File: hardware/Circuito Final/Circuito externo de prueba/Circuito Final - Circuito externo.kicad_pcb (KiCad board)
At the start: 2 copper layers, 163.8 x 129.8 mm, 18 parts, among them J1 Conn_02x19_Odd_Even, J2 Conn_02x19_Odd_Even, J3 Conn_01x02, J4 Conn_01x02, J5 Conn_01x02_Socket, SW1 SW_DIP_x04, SW2 SW_DIP_x04, SW4 SW_DIP_x01, SW5 SW_DIP_x01, SW6 SW_DIP_x01

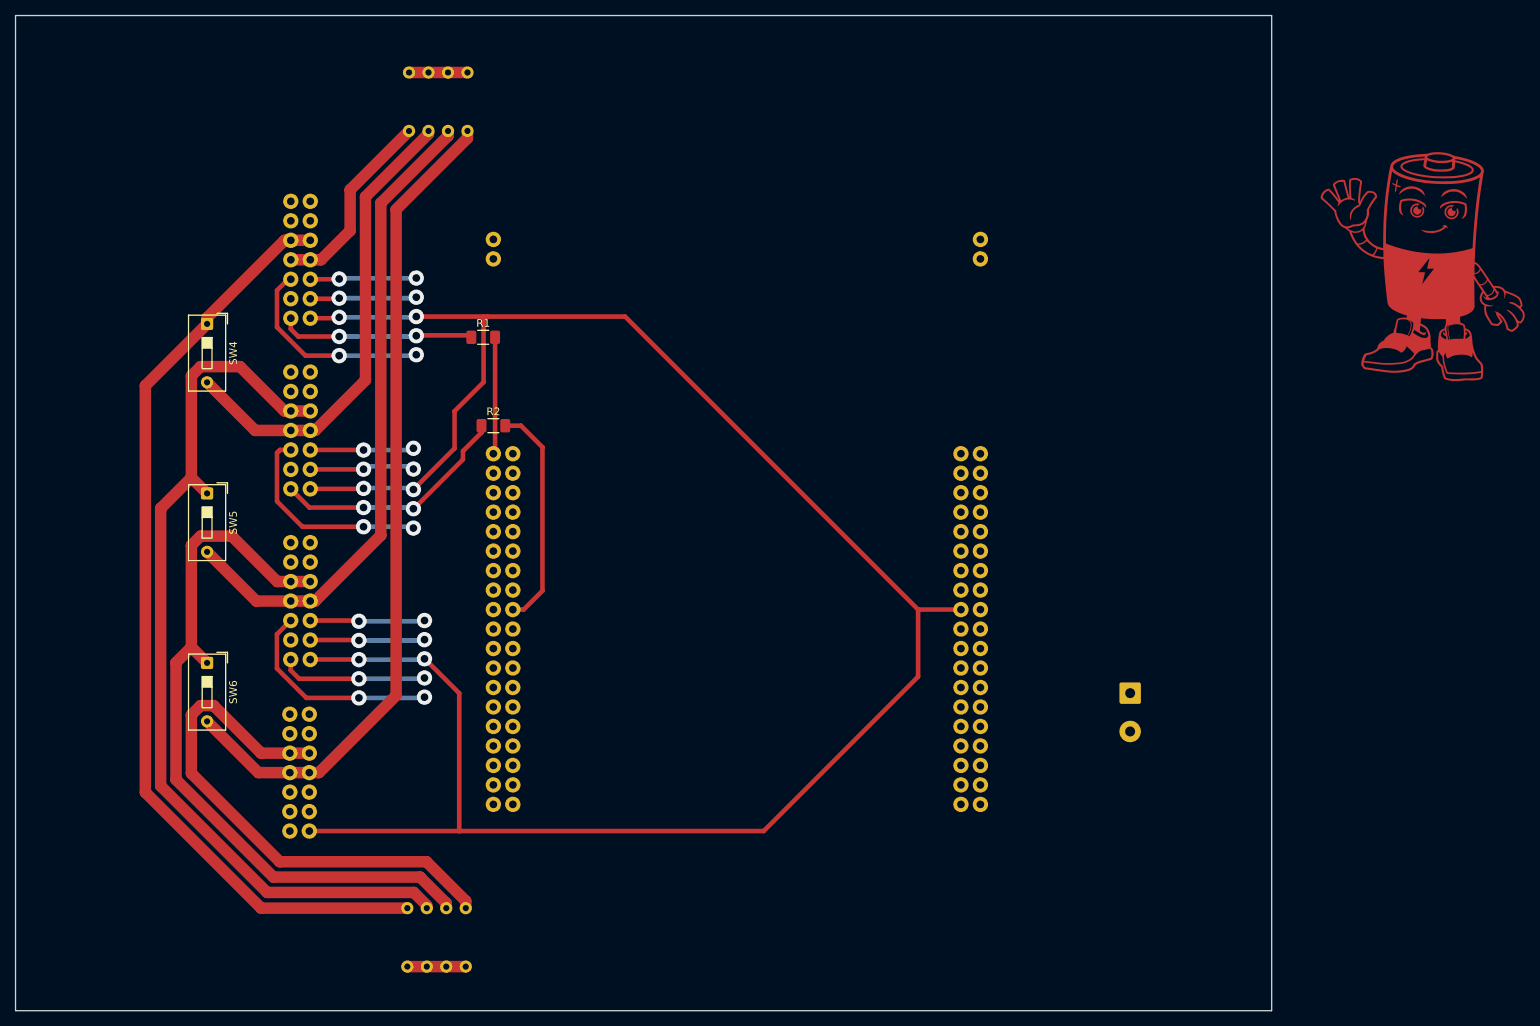
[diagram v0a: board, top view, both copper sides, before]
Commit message: subida de mediciones de switcheo con dos bancos, bitacora y kicad del circuito externo de prueba terminado
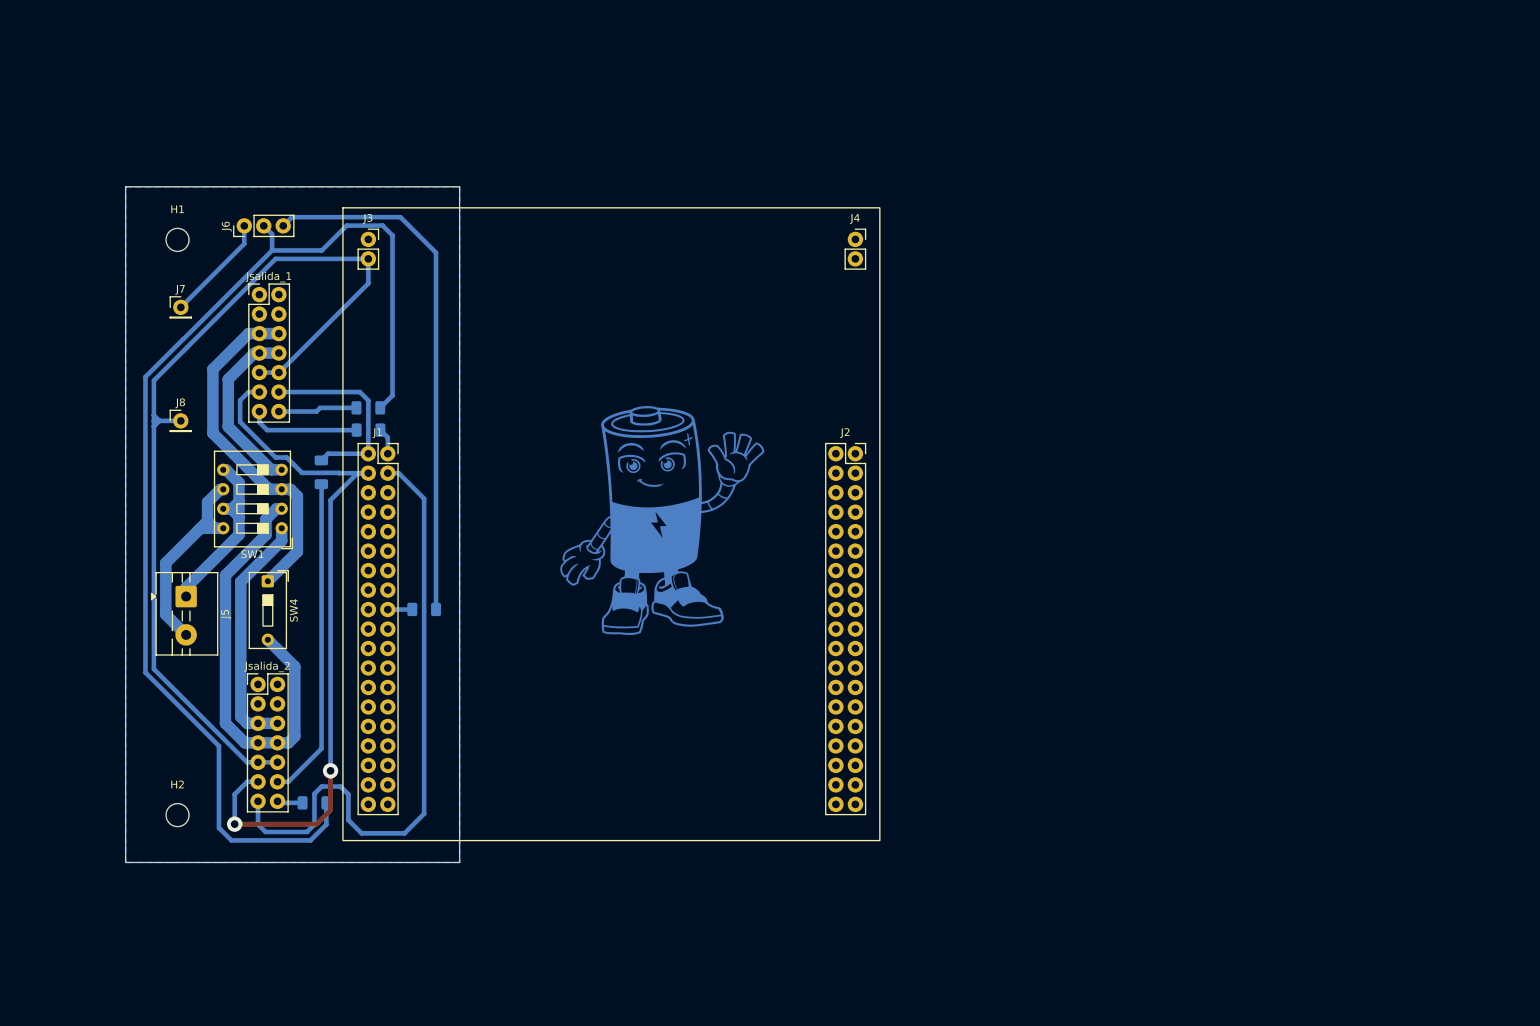
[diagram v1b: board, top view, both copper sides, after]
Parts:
- removed Jsalida_3, Jsalida_4: Conn_02x07_Odd_Even, Connector_PinHeader_2.54mm:PinHeader_2x07_P2.54mm_Vertical
- removed SW2: SW_DIP_x04, Button_Switch_THT:SW_DIP_SPSTx04_Slide_6.7x11.72mm_W7.62mm_P2.54mm_LowProfile
- removed SW5, SW6: SW_DIP_x01, Button_Switch_THT:SW_DIP_SPSTx01_Slide_9.78x4.72mm_W7.62mm_P2.54mm
- added H1: MountingHole, MountingHole:MountingHole_3mm, F.Cu at (73.1, 47.1)
- added H2: MountingHole, MountingHole:MountingHole_3mm, F.Cu at (73.1, 122.1)
- added J6: Conn_01x03_Pin, Connector_PinHeader_2.54mm:PinHeader_1x03_P2.54mm_Vertical, F.Cu at (81.8, 45.3)
- added J7: Conn_01x01, Connector_PinHeader_2.54mm:PinHeader_1x01_P2.54mm_Vertical, F.Cu at (73.5, 55.9)
- added J8: Conn_01x01, Connector_PinHeader_2.54mm:PinHeader_1x01_P2.54mm_Vertical, F.Cu at (73.5, 70.7)
- added R3: 0, Resistor_SMD:R_1206_3216Metric_Pad1.30x1.75mm_HandSolder, B.Cu at (98.0, 69.0)
- added R4: 0, Resistor_SMD:R_1206_3216Metric_Pad1.30x1.75mm_HandSolder, B.Cu at (105.3, 95.3)
- added R5: 0, Resistor_SMD:R_1206_3216Metric_Pad1.30x1.75mm_HandSolder, B.Cu at (91.0, 120.5)
- G***, R1, R2: moved to B.Cu
- J1, J2, J3, J4, J5, Jsalida_1, Jsalida_2, STM32: moved to F.Cu
- SW1: footprint Button_Switch_THT:SW_DIP_SPSTx04_Slide_6.7x11.72mm_W7.62mm_P2.54mm_LowProfile -> Button_Switch_THT:SW_DIP_SPSTx04_Slide_9.78x12.34mm_W7.62mm_P2.54mm; moved to F.Cu
- moved J5 123.7 mm to (74.2, 93.6)
- moved G*** 105.0 mm to (136.1, 84.0), turned to 180 degrees
- moved J3 79.8 mm to (98.0, 47.0), turned to 0 degrees
- moved J1 74.7 mm to (100.5, 75.0), turned to 0 degrees
- moved SW1 52.2 mm to (86.7, 84.7), turned to 180 degrees
- moved J2 47.2 mm to (161.5, 75.0), turned to 0 degrees
- moved J4 47.2 mm to (161.5, 47.0), turned to 0 degrees
- moved Jsalida_2 41.3 mm to (83.6, 105.1), turned to 0 degrees
- moved SW4 34.5 mm to (84.9, 91.6)
- moved R1 27.5 mm to (91.9, 77.4), turned to 90 degrees
- moved STM32 16.4 mm to (129.7, 84.2), turned to 0 degrees
- moved R2 16.3 mm to (98.0, 71.9), turned to 180 degrees
- moved Jsalida_1 13.9 mm to (83.8, 54.2), turned to 0 degrees
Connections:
- J1 pad 1: unconnected-(J1-Pin_1-Pad1) -> /Data_1
- J1 pad 17: /Vcc -> /Vcc_placa
- J1 pad 19: GND -> unconnected-(J1-Pin_19-Pad19)
- J1 pad 2: /Data_3 -> /clk_shift
- J1 pad 20: GND -> unconnected-(J1-Pin_20-Pad20)
- J1 pad 21: GND -> unconnected-(J1-Pin_21-Pad21)
- J1 pad 3: unconnected-(J1-Pin_3-Pad3) -> /Data_2
- J1 pad 4: /Data_4 -> /clk_latch
- J1 pad 7: GND -> unconnected-(J1-Pin_7-Pad7)
- J2 pad 1: /Data_1 -> unconnected-(J2-Pin_1-Pad1)
- J2 pad 10: GND -> unconnected-(J2-Pin_10-Pad10)
- J2 pad 18: /Data_2 -> unconnected-(J2-Pin_18-Pad18)
- J2 pad 19: GND -> unconnected-(J2-Pin_19-Pad19)
- J2 pad 3: /clk_shift -> unconnected-(J2-Pin_3-Pad3)
- J2 pad 31: GND -> unconnected-(J2-Pin_31-Pad31)
- J2 pad 5: /clk_latch -> unconnected-(J2-Pin_5-Pad5)
- J4 pad 2: GND -> unconnected-(J4-Pin_2-Pad2)
- Jsalida_1 pad 12: unconnected-(Jsalida_1-Pin_12-Pad12) -> /clk_shift
- Jsalida_1 pad 13: /Vcc -> /Data_1
- Jsalida_1 pad 14: /Data_1 -> /Vcc
- Jsalida_1 pad 9: /clk_shift -> GND
- Jsalida_2 pad 12: unconnected-(Jsalida_2-Pin_12-Pad12) -> /clk_shift
- Jsalida_2 pad 13: /Vcc -> /Data_2
- Jsalida_2 pad 14: /Data_2 -> /Vcc
- Jsalida_2 pad 9: /clk_shift -> GND
- R1 pad 1: /Data_1 -> /clk_shift
- R1 pad 2: /Data_1 -> /clk_shift
- R2 pad 1: /Data_2 -> /Data_1
- R2 pad 2: /Data_2 -> /Data_1
- SW1 pad 1: /bus_pos_1 -> /bus_pos_2
- SW1 pad 2: /bus_pos_2 -> /bus_neg_2
- SW1 pad 3: /bus_pos_3 -> /bus_pos_1
- SW1 pad 4: /bus_pos_4 -> /bus_neg_1
- SW1 pad 5: /bus_pos_salida -> /bus_neg_salida
- SW1 pad 7: /bus_pos_salida -> /bus_neg_salida
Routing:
- net /Vcc: track 276.4 -> 162.5 mm, vias 6 -> 0
- net /bus_neg_4: track 109.0 -> 0.00 mm
- net /bus_pos_3: track 95.3 -> 0.00 mm
- net /bus_pos_2: track 117.9 -> 32.0 mm
- net /bus_neg_3: track 85.2 -> 0.00 mm
- net /bus_pos_1: track 123.3 -> 46.0 mm
- net /Vcc_placa: track 0.00 -> 72.0 mm
- net /bus_pos_4: track 69.7 -> 0.00 mm
- net /clk_latch: track 42.3 -> 92.9 mm, vias 6 -> 2
- net GND: track 81.9 -> 121.1 mm, vias 6 -> 0
- net /clk_shift: track 42.2 -> 67.6 mm, vias 6 -> 0
- net /Data_1: track 40.9 -> 18.0 mm, vias 2 -> 0
- net /Data_2: track 61.2 -> 82.6 mm, vias 2 -> 0
- net /bus_pos_salida: track 7.62 -> 27.9 mm
- net /Data_3: track 19.2 -> 0.00 mm, vias 2 -> 0
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- added copper zone on B.Cu, net GND
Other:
- board size 163.8 x 129.8 mm -> 43.5 x 88.1 mm
